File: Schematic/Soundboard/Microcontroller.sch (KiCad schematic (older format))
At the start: 18 parts, among them J4 USB_B_Micro, J5 Conn_01x03_Male, J6 Conn_02x02_Counter_Clockwise, J7 Conn_ARM_JTAG_SWD_10, SW1 SW_Push, U1 STM32f429IIT6-units, U9 USBLC6-4SC6, Y1 Crystal_GND24

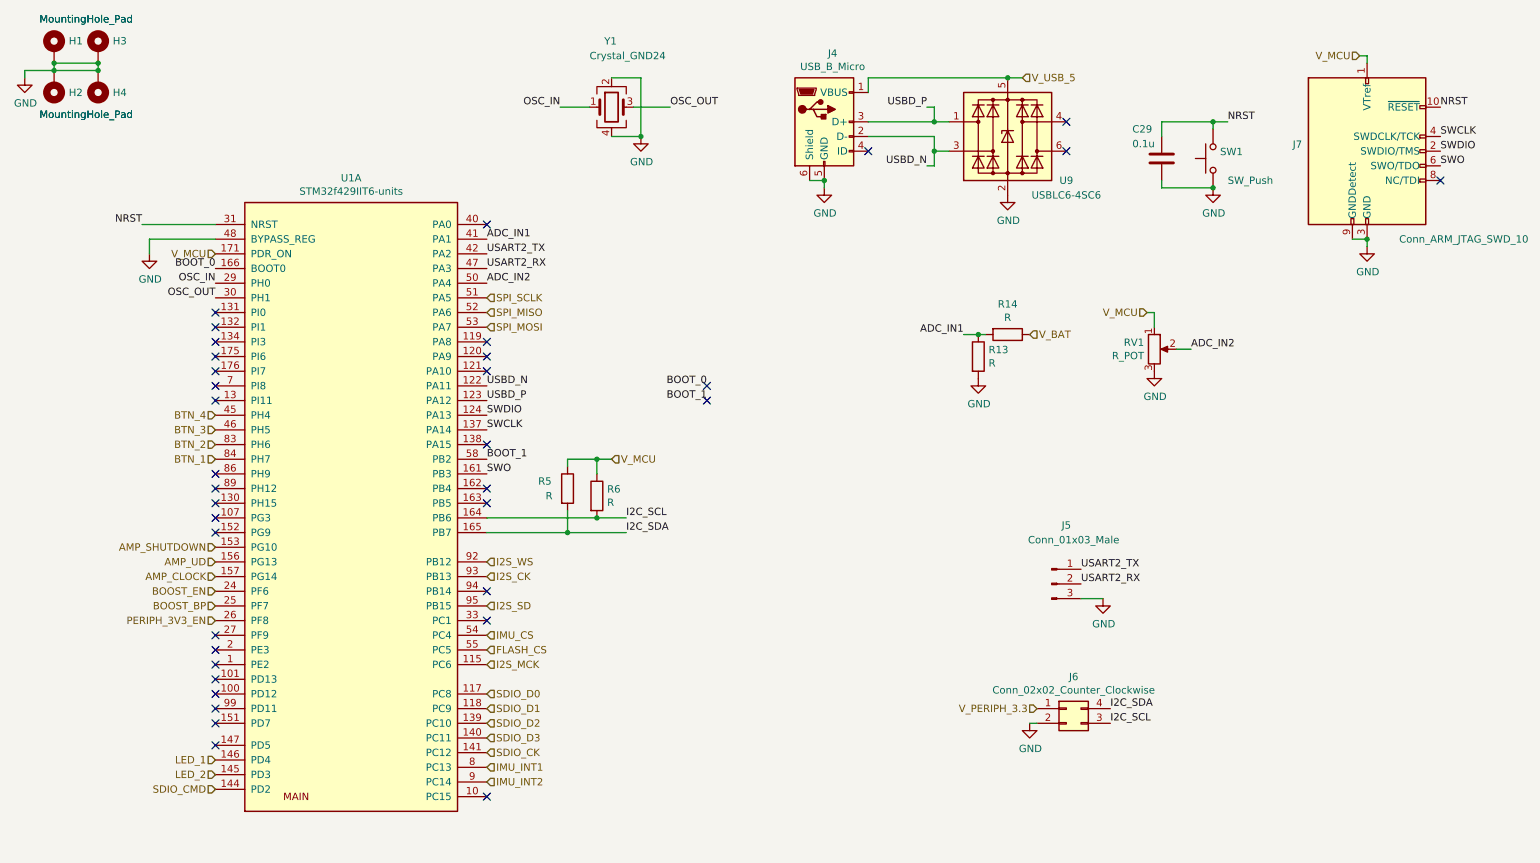
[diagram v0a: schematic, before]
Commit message: Complete connections except for display to be chosen
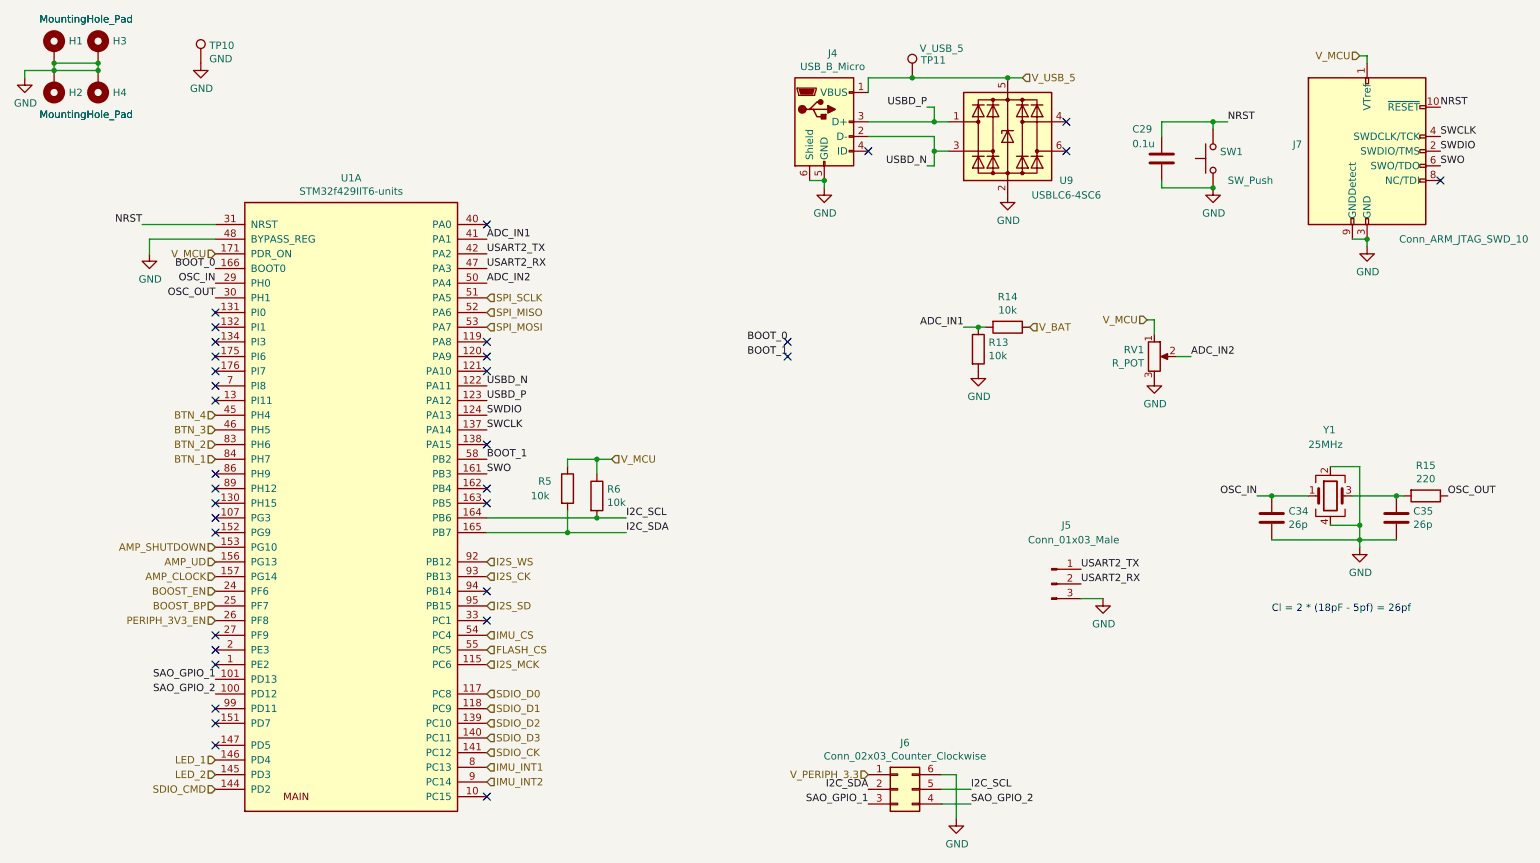
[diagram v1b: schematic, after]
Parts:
- removed J6: Conn_02x02_Counter_Clockwise, symbol Connector_Generic:Conn_02x02_Counter_Clockwise
- added C34, C35: 26p, symbol Device:C
- added J6: Conn_02x03_Counter_Clockwise, symbol Connector_Generic:Conn_02x03_Counter_Clockwise
- added R15: 220, symbol Device:R
- added TP10: GND, symbol Connector:TestPoint
- added TP11: V_USB_5, symbol Connector:TestPoint
- R13, R14, R5, R6: value R -> 10k
- Y1: value Crystal_GND24 -> 25MHz
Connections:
- net GND: now also C34.2, C35.2, J6.6 (Pin_6), TP10.1
- net I2C_SCL: now also J6.5 (Pin_5)
- net I2C_SDA: now also J6.2 (Pin_2)
- net OSC_IN: now also C34.1
- net OSC_OUT: now also R15.1; no longer Y1.3
- net V_PERIPH_3.3: now also J6.1 (Pin_1)
- net V_USB_5: now also TP11.1
- net SAO_GPIO_2: now reaches U1.100 (PD12)
- net SAO_GPIO_2: now also J6.4 (Pin_4)
- net SAO_GPIO_1: now reaches U1.101 (PD13)
- net SAO_GPIO_1: now also J6.3 (Pin_3)
- new net: C35.1, R15.2, Y1.3
- no-connect marks 36 -> 34
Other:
- note added: "Cl = 2 * (18pF - 5pf) = 26pf\n"
- moved on the sheet: R13, R14, RV1, Y1

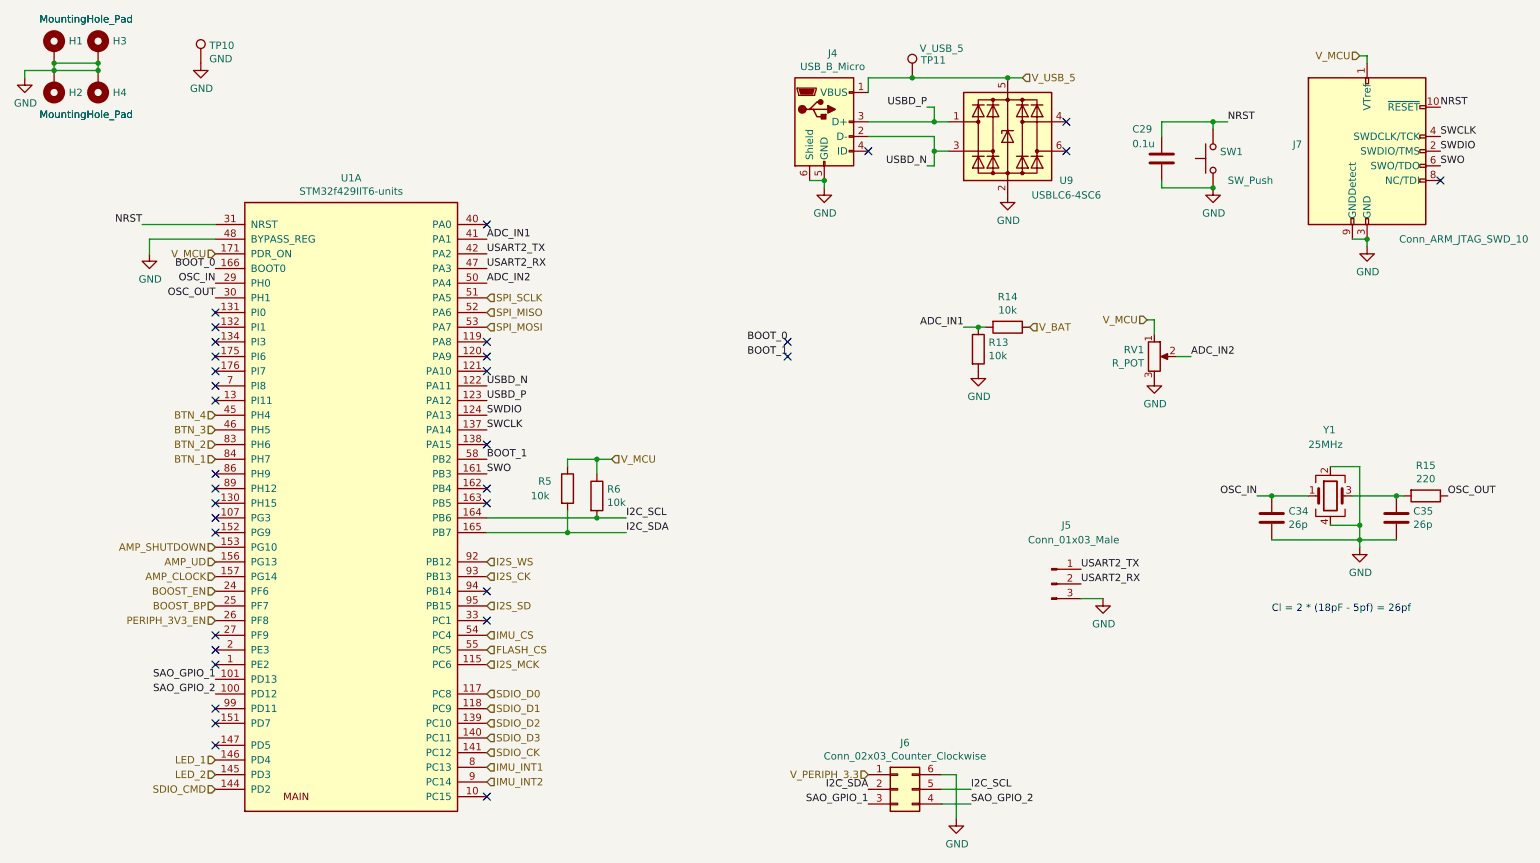
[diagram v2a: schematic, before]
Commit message: Choose display. Complete schematic
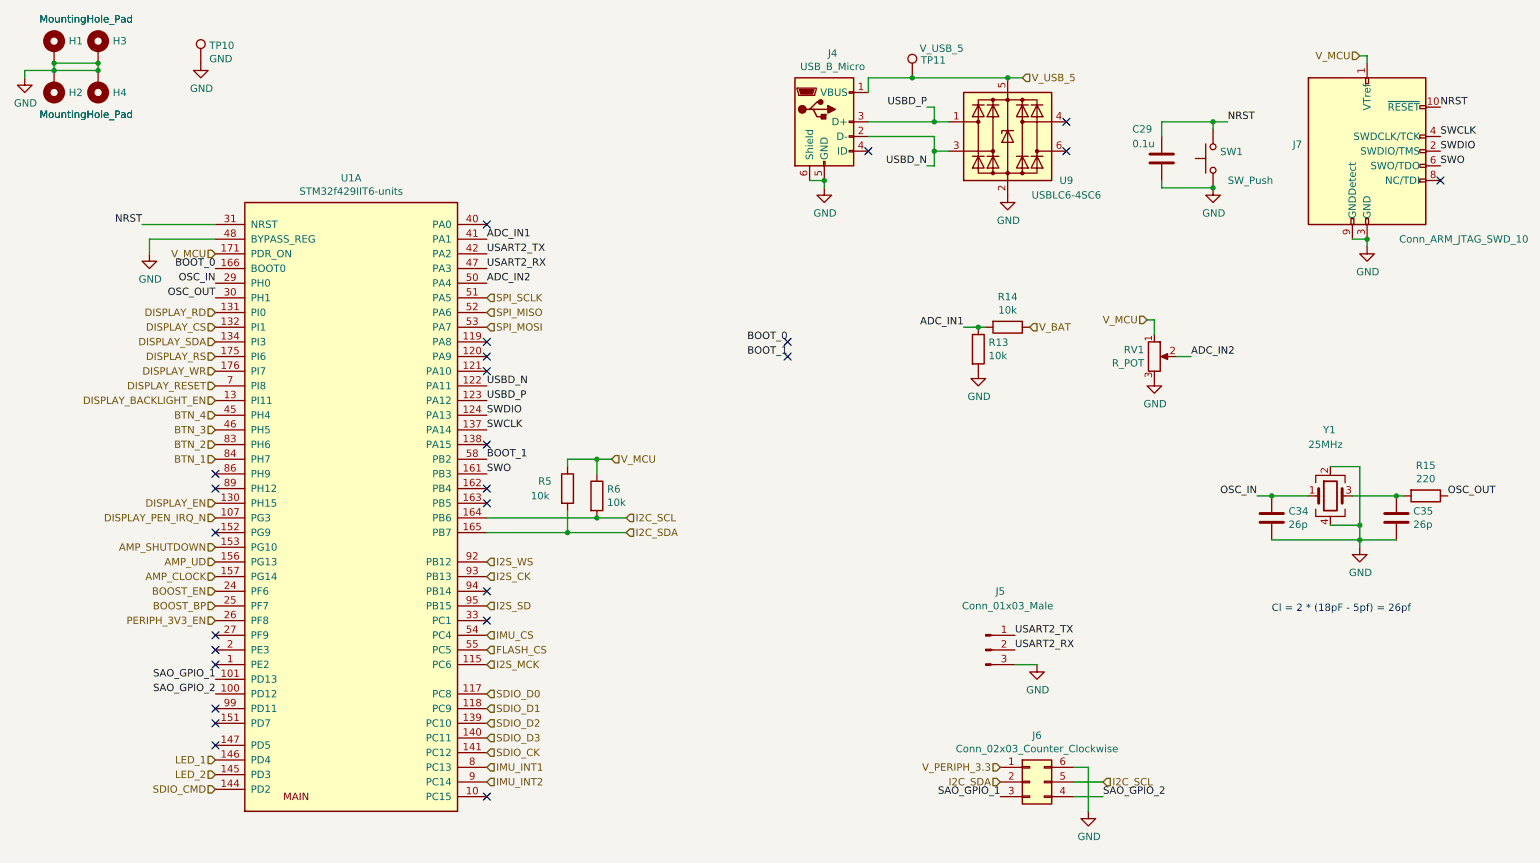
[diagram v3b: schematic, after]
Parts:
- C29, C34, C35: footprint (none) -> Capacitor_SMD:C_0603_1608Metric_Pad1.05x0.95mm_HandSolder
- H1, H2, H3, H4: footprint (none) -> MountingHole:MountingHole_2.5mm_Pad_Via
- J5: footprint (none) -> Connector_PinHeader_1.27mm:PinHeader_1x03_P1.27mm_Vertical
- J6: footprint (none) -> Connector_PinHeader_1.27mm:PinHeader_2x03_P1.27mm_Vertical
- R13, R14, R15, R5, R6: footprint (none) -> Resistor_SMD:R_0603_1608Metric_Pad1.05x0.95mm_HandSolder
- RV1: footprint (none) -> Potentiometer_THT:Potentiometer_Bourns_3339P_Vertical
- TP10, TP11: footprint (none) -> TestPoint:TestPoint_Pad_D2.0mm
- U1: footprint (none) -> Package_QFP:LQFP-176_24x24mm_P0.5mm
- Y1: footprint (none) -> Crystal:Crystal_SMD_3225-4Pin_3.2x2.5mm
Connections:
- net DISPLAY_PEN_IRQ_N: now reaches U1.107 (PG3)
- net DISPLAY_BACKLIGHT_EN: now reaches U1.13 (PI11)
- net DISPLAY_EN: now reaches U1.130 (PH15)
- net DISPLAY_RD: now reaches U1.131 (PI0)
- net DISPLAY_CS: now reaches U1.132 (PI1)
- net DISPLAY_SDA: now reaches U1.134 (PI3)
- net DISPLAY_RS: now reaches U1.175 (PI6)
- net DISPLAY_WR: now reaches U1.176 (PI7)
- net DISPLAY_RESET: now reaches U1.7 (PI8)
- no-connect marks 34 -> 25
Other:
- moved on the sheet: J5, J6
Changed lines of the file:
@@
 $Descr A4 11693 8268
 encoding utf-8
-Sheet 6 7
+Sheet 7 7
 Title ""
 Date ""
@@
 Text Label 10450 1300 0    50   ~ 0
 NRST
-Text Label 4900 4100 0    50   ~ 0
-I2C_SCL
-Text Label 4900 4200 0    50   ~ 0
-I2C_SDA
 Text Label 3950 2300 0    50   ~ 0
 USART2_TX
@@
 L power:GND #PWR023
 U 1 1 5F66059D
-P 7150 6150
-F 0 "#PWR023" H 7150 5900 50  0001 C CNN
-F 1 "GND" H 7155 5977 50  0000 C CNN
-F 2 "" H 7150 6150 50  0001 C CNN
-F 3 "" H 7150 6150 50  0001 C CNN
-	1    7150 6150
+P 8050 6100
+F 0 "#PWR023" H 8050 5850 50  0001 C CNN
+F 1 "GND" H 8055 5927 50  0000 C CNN
+F 2 "" H 8050 6100 50  0001 C CNN
+F 3 "" H 8050 6100 50  0001 C CNN
+	1    8050 6100
 	1    0    0    -1
 $EndComp
@@
 	1    0    0    -1
 $EndComp
-Text HLabel 6550 5850 0    50   Input ~ 0
+Text HLabel 7450 5800 0    50   Input ~ 0
 V_PERIPH_3.3
 Text HLabel 9900 950  0    50   Input ~ 0
@@
 F 0 "Y1" H 9650 4400 50  0000 L CNN
 F 1 "25MHz" H 9550 4300 50  0000 L CNN
-F 2 "" H 9700 3950 50  0001 C CNN
+F 2 "Crystal:Crystal_SMD_3225-4Pin_3.2x2.5mm" H 9700 3950 50  0001 C CNN
 F 3 "~" H 9700 3950 50  0001 C CNN
 	1    9700 3950
@@
 F 0 "R6" H 4770 3996 50  0000 L CNN
 F 1 "10k" H 4770 3905 50  0000 L CNN
-F 2 "" V 4630 3950 50  0001 C CNN
+F 2 "Resistor_SMD:R_0603_1608Metric_Pad1.05x0.95mm_HandSolder" V 4630 3950 50  0001 C CNN
 F 3 "~" H 4700 3950 50  0001 C CNN
 	1    4700 3950
@@
 F 0 "R5" H 4300 3950 50  0000 L CNN
 F 1 "10k" H 4250 3850 50  0000 L CNN
-F 2 "" V 4430 3900 50  0001 C CNN
+F 2 "Resistor_SMD:R_0603_1608Metric_Pad1.05x0.95mm_HandSolder" V 4430 3900 50  0001 C CNN
 F 3 "~" H 4500 3900 50  0001 C CNN
 	1    4500 3900
@@
 Text HLabel 2100 4300 0    50   Input ~ 0
 AMP_SHUTDOWN
-Text Label 8000 4450 0    50   ~ 0
+Text Label 7550 4900 0    50   ~ 0
 USART2_TX
-Text Label 8000 4550 0    50   ~ 0
+Text Label 7550 5000 0    50   ~ 0
 USART2_RX
 $Comp
 L Connector:Conn_01x03_Male J5
 U 1 1 5F49C5BF
-P 7800 4550
-F 0 "J5" H 7900 4950 50  0000 C CNN
-F 1 "Conn_01x03_Male" H 7950 4850 50  0000 C CNN
-F 2 "" H 7800 4550 50  0001 C CNN
-F 3 "~" H 7800 4550 50  0001 C CNN
-	1    7800 4550
+P 7350 5000
+F 0 "J5" H 7450 5400 50  0000 C CNN
+F 1 "Conn_01x03_Male" H 7500 5300 50  0000 C CNN
+F 2 "Connector_PinHeader_1.27mm:PinHeader_1x03_P1.27mm_Vertical" H 7350 5000 50  0001 C CNN
+F 3 "~" H 7350 5000 50  0001 C CNN
+	1    7350 5000
 	1    0    0    -1
 $EndComp
@@
 L power:GND #PWR024
 U 1 1 5F49E6A4
-P 8150 4650
-F 0 "#PWR024" H 8150 4400 50  0001 C CNN
-F 1 "GND" H 8155 4477 50  0000 C CNN
-F 2 "" H 8150 4650 50  0001 C CNN
-F 3 "" H 8150 4650 50  0001 C CNN
-	1    8150 4650
-	1    0    0    -1
-$EndComp
-Wire Wire Line
-	8000 4650 8150 4650
+P 7700 5100
+F 0 "#PWR024" H 7700 4850 50  0001 C CNN
+F 1 "GND" H 7705 4927 50  0000 C CNN
+F 2 "" H 7700 5100 50  0001 C CNN
+F 3 "" H 7700 5100 50  0001 C CNN
+	1    7700 5100
+	1    0    0    -1
+$EndComp
+Wire Wire Line
+	7550 5100 7700 5100
 $Comp
 L Device:C C29
@@
 F 0 "C29" H 8350 1850 50  0000 L CNN
 F 1 "0.1u" H 8350 1750 50  0000 L CNN
-F 2 "" H 8588 1500 50  0001 C CNN
+F 2 "Capacitor_SMD:C_0603_1608Metric_Pad1.05x0.95mm_HandSolder" H 8588 1500 50  0001 C CNN
 F 3 "~" H 8550 1650 50  0001 C CNN
 	1    8550 1650
@@
 F 0 "H1" H 1100 951 50  0000 L CNN
 F 1 "MountingHole_Pad" H 900 450 50  0000 L CNN
-F 2 "" H 1000 900 50  0001 C CNN
+F 2 "MountingHole:MountingHole_2.5mm_Pad_Via" H 1000 900 50  0001 C CNN
 F 3 "~" H 1000 900 50  0001 C CNN
 	1    1000 900
@@
 F 0 "H3" H 1400 951 50  0000 L CNN
 F 1 "MountingHole_Pad" H 900 450 50  0000 L CNN
-F 2 "" H 1300 900 50  0001 C CNN
+F 2 "MountingHole:MountingHole_2.5mm_Pad_Via" H 1300 900 50  0001 C CNN
 F 3 "~" H 1300 900 50  0001 C CNN
 	1    1300 900
@@
 F 0 "H2" H 1100 1201 50  0000 L CNN
 F 1 "MountingHole_Pad" H 900 700 50  0000 L CNN
-F 2 "" H 1000 1150 50  0001 C CNN
+F 2 "MountingHole:MountingHole_2.5mm_Pad_Via" H 1000 1150 50  0001 C CNN
 F 3 "~" H 1000 1150 50  0001 C CNN
 	1    1000 1150
@@
 F 0 "H4" H 1400 1201 50  0000 L CNN
 F 1 "MountingHole_Pad" H 900 700 50  0000 L CNN
-F 2 "" H 1300 1150 50  0001 C CNN
+F 2 "MountingHole:MountingHole_2.5mm_Pad_Via" H 1300 1150 50  0001 C CNN
 F 3 "~" H 1300 1150 50  0001 C CNN
 	1    1300 1150
@@
 Text HLabel 2100 3400 0    50   Input ~ 0
 BTN_4
-NoConn ~ 2100 2700
-NoConn ~ 2100 2800
-NoConn ~ 2100 2900
-NoConn ~ 2100 3000
-NoConn ~ 2100 3100
-NoConn ~ 2100 3200
-NoConn ~ 2100 3300
 NoConn ~ 2100 3800
 NoConn ~ 2100 3900
-NoConn ~ 2100 4000
-NoConn ~ 2100 4100
 NoConn ~ 2100 4200
 NoConn ~ 2100 4900
@@
 F 0 "U1" H 3025 1817 50  0000 C CNN
 F 1 "STM32f429IIT6-units" H 3025 1726 50  0000 C CNN
-F 2 "" H 2850 1800 50  0001 C CNN
+F 2 "Package_QFP:LQFP-176_24x24mm_P0.5mm" H 2850 1800 50  0001 C CNN
 F 3 "" H 2850 1800 50  0001 C CNN
 	1    2850 1800
 	1    0    0    -1
 $EndComp
-Text Label 7250 5950 0    50   ~ 0
-I2C_SCL
-Text Label 6550 5950 2    50   ~ 0
-I2C_SDA
 Text Label 6000 2900 2    50   ~ 0
 BOOT_0
@@
 F 0 "R14" V 7293 2800 50  0000 C CNN
 F 1 "10k" V 7384 2800 50  0000 C CNN
-F 2 "" V 7430 2800 50  0001 C CNN
+F 2 "Resistor_SMD:R_0603_1608Metric_Pad1.05x0.95mm_HandSolder" V 7430 2800 50  0001 C CNN
 F 3 "~" H 7500 2800 50  0001 C CNN
 	1    7500 2800
@@
 F 0 "R13" H 7370 2996 50  0000 L CNN
 F 1 "10k" H 7370 2905 50  0000 L CNN
-F 2 "" V 7230 2950 50  0001 C CNN
+F 2 "Resistor_SMD:R_0603_1608Metric_Pad1.05x0.95mm_HandSolder" V 7230 2950 50  0001 C CNN
 F 3 "~" H 7300 2950 50  0001 C CNN
 	1    7300 2950
@@
 F 0 "RV1" H 8430 3046 50  0000 R CNN
 F 1 "R_POT" H 8430 2955 50  0000 R CNN
-F 2 "" H 8500 3000 50  0001 C CNN
+F 2 "Potentiometer_THT:Potentiometer_Bourns_3339P_Vertical" H 8500 3000 50  0001 C CNN
 F 3 "~" H 8500 3000 50  0001 C CNN
 	1    8500 3000
@@
 F 0 "C34" H 9415 4146 50  0000 L CNN
 F 1 "26p" H 9415 4055 50  0000 L CNN
-F 2 "" H 9338 3950 50  0001 C CNN
+F 2 "Capacitor_SMD:C_0603_1608Metric_Pad1.05x0.95mm_HandSolder" H 9338 3950 50  0001 C CNN
 F 3 "~" H 9300 4100 50  0001 C CNN
 	1    9300 4100
@@
 F 0 "C35" H 10265 4146 50  0000 L CNN
 F 1 "26p" H 10265 4055 50  0000 L CNN
-F 2 "" H 10188 3950 50  0001 C CNN
+F 2 "Capacitor_SMD:C_0603_1608Metric_Pad1.05x0.95mm_HandSolder" H 10188 3950 50  0001 C CNN
 F 3 "~" H 10150 4100 50  0001 C CNN
 	1    10150 4100
@@
 F 0 "R15" V 10143 3950 50  0000 C CNN
 F 1 "220" V 10234 3950 50  0000 C CNN
-F 2 "" V 10280 3950 50  0001 C CNN
+F 2 "Resistor_SMD:R_0603_1608Metric_Pad1.05x0.95mm_HandSolder" V 10280 3950 50  0001 C CNN
 F 3 "~" H 10350 3950 50  0001 C CNN
 	1    10350 3950
@@
 F 0 "TP11" H 6908 1220 50  0000 L CNN
 F 1 "V_USB_5" H 6900 1300 50  0000 L CNN
-F 2 "" H 7050 1100 50  0001 C CNN
+F 2 "TestPoint:TestPoint_Pad_D2.0mm" H 7050 1100 50  0001 C CNN
 F 3 "~" H 7050 1100 50  0001 C CNN
 	1    6850 1100
@@
 L Connector_Generic:Conn_02x03_Counter_Clockwise J6
 U 1 1 5F71C253
-P 6750 5950
-F 0 "J6" H 6800 6267 50  0000 C CNN
-F 1 "Conn_02x03_Counter_Clockwise" H 6800 6176 50  0000 C CNN
-F 2 "" H 6750 5950 50  0001 C CNN
-F 3 "~" H 6750 5950 50  0001 C CNN
-	1    6750 5950
-	1    0    0    -1
-$EndComp
-Wire Wire Line
-	7150 6150 7150 5850
-Wire Wire Line
-	7150 5850 7050 5850
-Wire Wire Line
-	7250 5950 7050 5950
-Text Label 6550 6050 2    50   ~ 0
+P 7650 5900
+F 0 "J6" H 7700 6217 50  0000 C CNN
+F 1 "Conn_02x03_Counter_Clockwise" H 7700 6126 50  0000 C CNN
+F 2 "Connector_PinHeader_1.27mm:PinHeader_2x03_P1.27mm_Vertical" H 7650 5900 50  0001 C CNN
+F 3 "~" H 7650 5900 50  0001 C CNN
+	1    7650 5900
+	1    0    0    -1
+$EndComp
+Wire Wire Line
+	8050 6100 8050 5800
+Wire Wire Line
+	8050 5800 7950 5800
+Wire Wire Line
+	8150 5900 7950 5900
+Text Label 7450 6000 2    50   ~ 0
 SAO_GPIO_1
-Text Label 7250 6050 0    50   ~ 0
+Text Label 8150 6000 0    50   ~ 0
 SAO_GPIO_2
 Wire Wire Line
-	7250 6050 7050 6050
+	8150 6000 7950 6000
 Text Label 2100 5200 2    50   ~ 0
 SAO_GPIO_1
@@
 F 0 "TP10" H 2058 1120 50  0000 L CNN
 F 1 "GND" H 2058 1029 50  0000 L CNN
-F 2 "" H 2200 1000 50  0001 C CNN
+F 2 "TestPoint:TestPoint_Pad_D2.0mm" H 2200 1000 50  0001 C CNN
 F 3 "~" H 2200 1000 50  0001 C CNN
 	1    2000 1000
@@
 	1    0    0    -1
 $EndComp
+Text HLabel 2100 2700 0    50   Input ~ 0
+DISPLAY_RD
+Text HLabel 2100 2800 0    50   Input ~ 0
+DISPLAY_CS
+Text HLabel 2100 4000 0    50   Input ~ 0
+DISPLAY_EN
+Text HLabel 2100 2900 0    50   Input ~ 0
+DISPLAY_SDA
+Text HLabel 2100 3000 0    50   Input ~ 0
+DISPLAY_RS
+Text HLabel 2100 3100 0    50   Input ~ 0
+DISPLAY_WR
+Text HLabel 2100 4100 0    50   Input ~ 0
+DISPLAY_PEN_IRQ_N
+Text HLabel 2100 3300 0    50   Input ~ 0
+DISPLAY_BACKLIGHT_EN
+Text HLabel 7450 5900 0    50   Input ~ 0
+I2C_SDA
+Text HLabel 8150 5900 2    50   Input ~ 0
+I2C_SCL
+Text HLabel 4900 4200 2    50   Input ~ 0
+I2C_SDA
+Text HLabel 4900 4100 2    50   Input ~ 0
+I2C_SCL
+Text HLabel 2100 3200 0    50   Input ~ 0
+DISPLAY_RESET
 $EndSCHEMATC
